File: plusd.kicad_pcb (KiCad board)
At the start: 2 copper layers, 99.1 x 99.1 mm, 63 parts, among them J1 ZX_Spectrum_Connector_GENERIC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, J4 Conn_02x17_Odd_Even, J6 Conn_02x13_Odd_Even, SW1 SW_DPST_x2, SW2 SW_DIP_x02, SW3 SW_DPST_x2, U1 74LS27, U10 74LS374, U11 74LS126, U12 GAL22V10, U2 PAL20L8, U3 74LS00, U4 L7805, U5 AT28C256, U6 6264, U7 WD1772, U8 74LS175, U9 74LS06, Y1 8.000Mhz

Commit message: ahora con joystick
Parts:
- moved R7 0.64 mm to (74.3, 61.0)
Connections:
- J4 pad 26: /DS1 -> /TRACK_0
- R6 pad 1: /DS1 -> /TRACK_0
- U7 pad 23: /DS1 -> /TRACK_0
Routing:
- net /DS1: track 104.3 -> 54.0 mm
- net /TRACK_0: track 0.00 -> 45.6 mm
- net Net-(JP4-Pad1): track 13.1 -> 7.22 mm
- net Net-(C17-Pad2): track 35.9 -> 36.7 mm

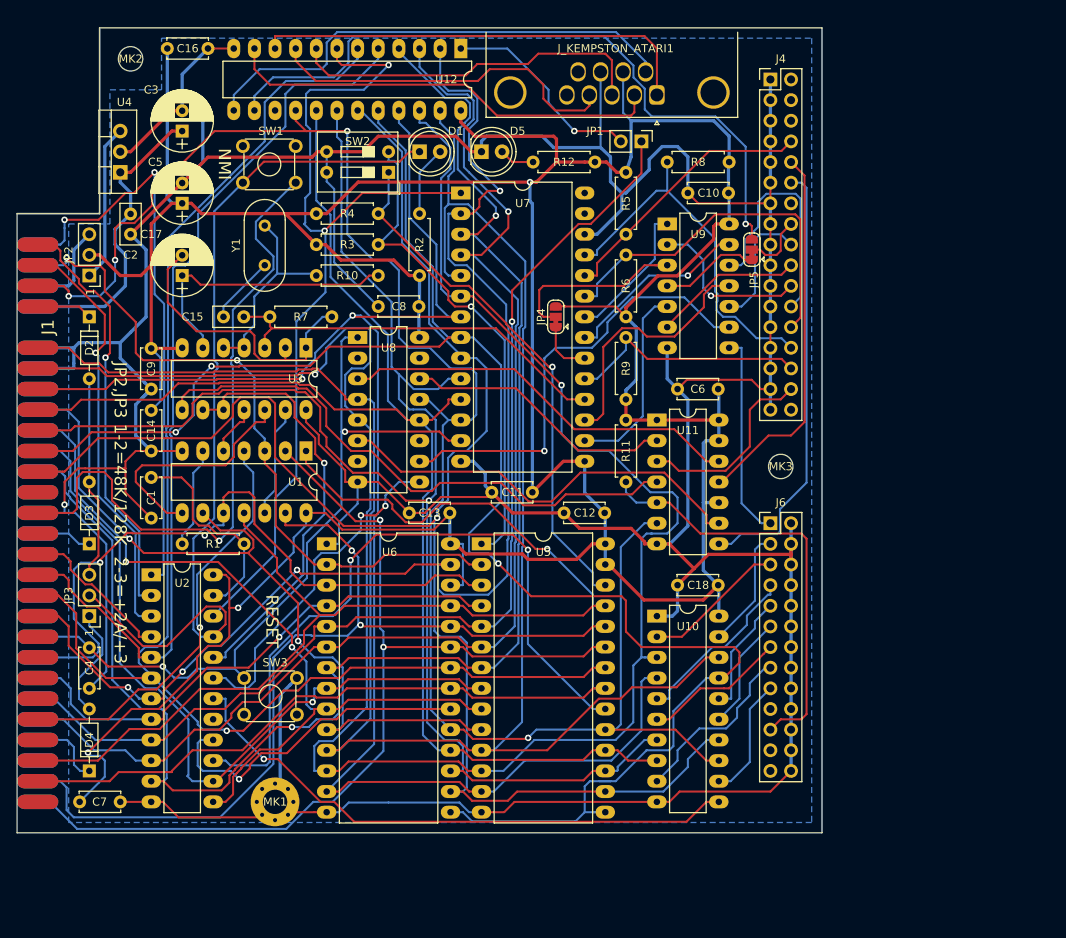
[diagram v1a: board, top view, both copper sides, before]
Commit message: add cable jumpers
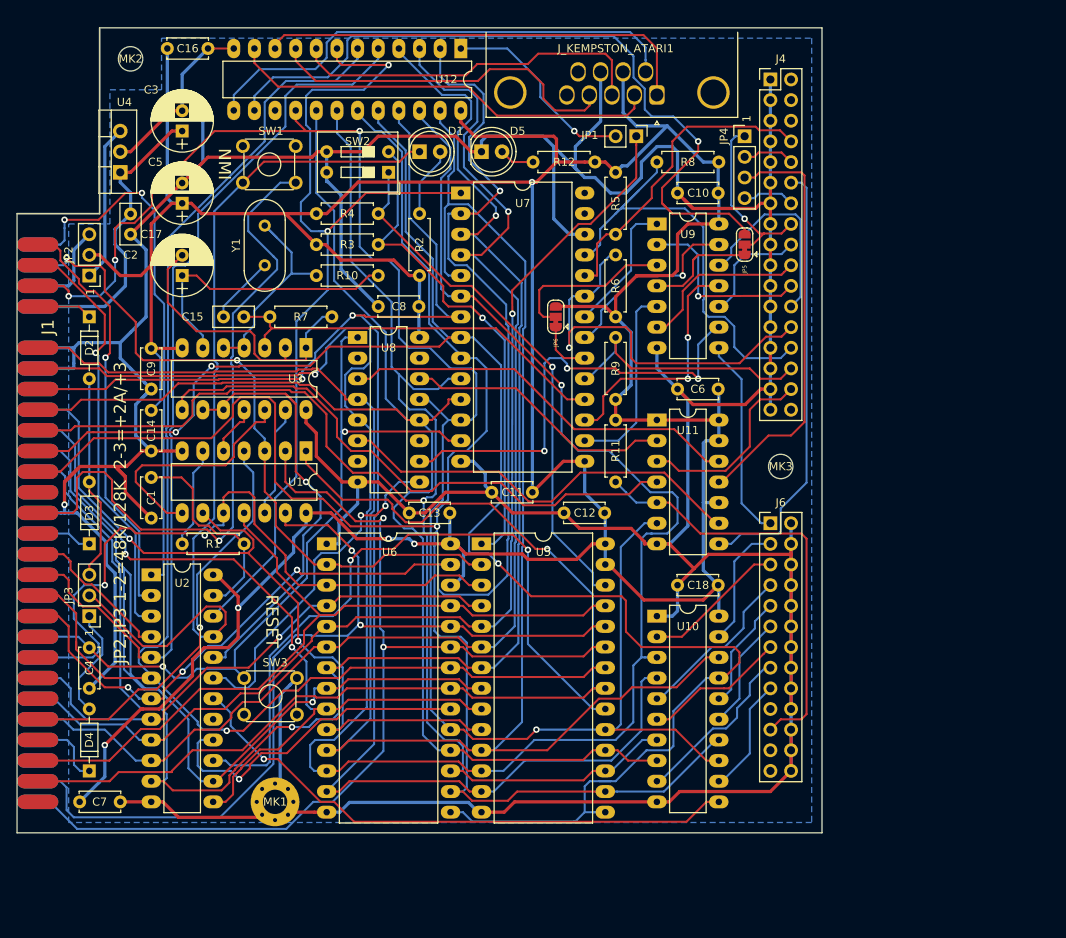
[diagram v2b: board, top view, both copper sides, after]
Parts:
- added JP4: Conn_01x04_Male, Connector_PinHeader_2.54mm:PinHeader_1x04_P2.54mm_Vertical, F.Cu at (125.1, 38.7)
- moved C10 1.27 mm to (116.8, 45.7)
- moved R11 1.27 mm to (109.2, 81.3)
- moved R5 1.27 mm to (109.2, 50.8)
- moved R6 1.27 mm to (109.2, 53.3)
- moved R8 1.27 mm to (114.3, 41.9)
- moved R9 1.27 mm to (109.2, 63.5)
- moved U9 1.27 mm to (114.3, 49.5)
- moved JP5 1.08 mm to (125.1, 52.1)
- moved JP1 0.90 mm to (111.8, 38.7)
- renumbered JP4 to JP6
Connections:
- J4 pad 10: /DS0 -> Net-(J2-Pad2)
- J4 pad 14: (no net) -> Net-(J2-Pad4)
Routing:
- net /A2: track 93.3 -> 116.3 mm
- net /MOTOR_ON: track 7.86 -> 22.1 mm, vias 0 -> 1
- net GND: track 658.0 -> 670.8 mm
- net Net-(J4-Pad28): track 45.7 -> 56.3 mm
- net Net-(J2-Pad4): track 0.00 -> 6.43 mm
- net Net-(J2-Pad2): track 0.00 -> 6.43 mm
- net ALT_MOTOR_ON: track 86.8 -> 92.4 mm
- net /INDEX: track 33.1 -> 38.6 mm
- net /DS0: track 46.3 -> 51.7 mm
- net Net-(J4-Pad24): track 29.8 -> 24.7 mm
- net /D6: track 171.9 -> 176.9 mm
- net /TRACK_0: track 45.6 -> 50.4 mm, vias 0 -> 1
- net /A14: track 71.2 -> 66.7 mm
- net /A11: track 120.1 -> 123.2 mm
- net Net-(J4-Pad30): track 30.0 -> 33.1 mm
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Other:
- net class power: trace_width 0.35 -> 0.4

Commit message: fix power to chips
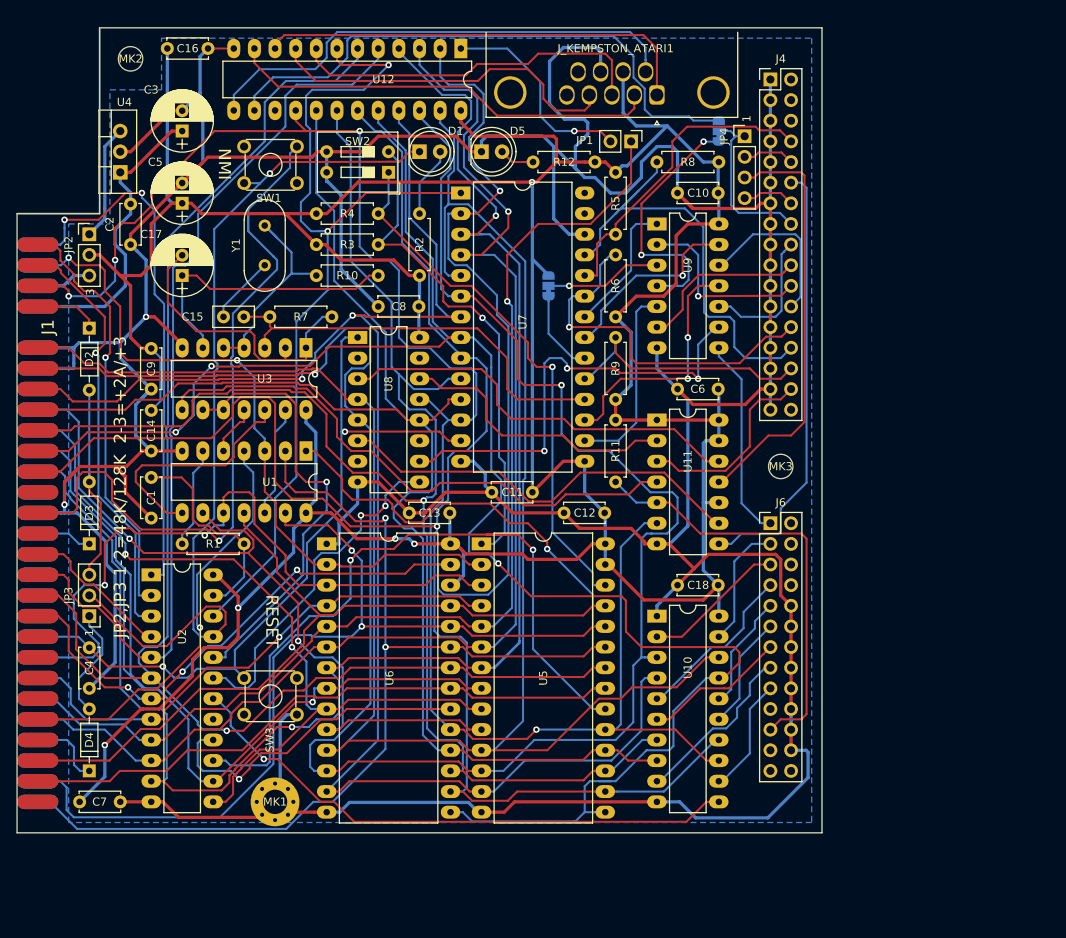
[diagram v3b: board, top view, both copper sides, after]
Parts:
- C2: value 10n -> 100n; footprint Capacitors_THT:C_Disc_D5.0mm_W2.5mm_P2.50mm -> Capacitors_THT:C_Disc_D5.0mm_W2.5mm_P5.00mm
- JP5, JP6: moved to B.Cu
- R12, R2: value 2K2 -> 680
- SW1, SW3: footprint Buttons_Switches_THT:SW_TH_Tactile_Omron_B3F-10xx -> SINCLAIR:SW_TH_Tactile_Omron_B3F-10xx
- moved JP5 14.3 mm to (121.9, 38.1)
- moved SW1 7.75 mm to (63.5, 40.0), turned to 0 degrees
- moved JP2 5.08 mm to (44.5, 50.8), turned to 0 degrees
- moved JP6 3.91 mm to (101.0, 57.1)
- moved D2 1.40 mm to (44.5, 62.4)
- moved C2 1.27 mm to (49.5, 52.1)
- moved JP1 0.90 mm to (111.1, 39.4)
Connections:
- J6 pad 2: GND -> (no net)
- J6 pad 26: GND -> (no net)
- J6 pad 4: GND -> (no net)
- J6 pad 6: GND -> (no net)
- J6 pad 8: GND -> (no net)
- SW3 pad 1: /RESET -> (no net)
- SW3 pad 2: GND -> (no net)
- SW3 pad 3: (no net) -> /RESET
- SW3 pad 4: (no net) -> GND
- U3 pad 14: GND -> +5V
- U3 pad 7: +5V -> GND
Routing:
- net GND: track 670.8 -> 639.1 mm, vias 1 -> 2
- net ALT_MOTOR_ON: track 92.4 -> 70.6 mm, vias 1 -> 0
- net Net-(JP5-Pad1): track 14.2 -> 31.7 mm, vias 0 -> 2
- net /A3: track 197.8 -> 207.5 mm
- net Net-(JP6-Pad2): track 21.0 -> 14.6 mm, vias 0 -> 1
- net NMI: track 83.8 -> 89.4 mm
- net Net-(JP2-Pad1): track 19.4 -> 13.8 mm
- net /TRACK_0: track 50.4 -> 45.7 mm
- net plus3_5V: track 11.2 -> 6.88 mm
- net Net-(J4-Pad24): track 24.7 -> 20.6 mm
- net ROM_CS: track 86.4 -> 89.9 mm
- net Net-(JP6-Pad1): track 7.22 -> 10.3 mm
- net /DIR: track 14.1 -> 17.2 mm
- net /A4: track 155.6 -> 158.4 mm
- net /D1: track 251.1 -> 253.8 mm
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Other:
- board text added: "1773 1772"
- board text added: "3"
- board text added: "EMU REAL"
- board text added: "Expecial Edicion for www.va-de-retro.com"
- board text removed: "Edicion para www.va-de-retro.com"

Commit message: add schematic and BOM
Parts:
- removed MK3: Mounting_Hole, MountingHole:MountingHole_3mm
- added JP7: Conn_02x02_Odd_Even, Connector_PinHeader_2.54mm:PinHeader_2x02_P2.54mm_Vertical, F.Cu at (129.0, 81.5)
- SW1, SW3: footprint SINCLAIR:SW_TH_Tactile_Omron_B3F-10xx -> Buttons_Switches_THT:SW_TH_Tactile_Omron_B3F-10xx
- moved J_KEMPSTON_ATARI1 1.91 mm to (114.3, 31.8)
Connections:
- U11 pad 11: /DS0 -> Net-(JP7-Pad3)
- U11 pad 8: /DS1 -> Net-(JP7-Pad2)
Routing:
- net Net-(JP7-Pad2): track 0.00 -> 15.4 mm
- net /DS1: track 54.0 -> 40.8 mm
- net Net-(JP7-Pad3): track 0.00 -> 8.42 mm
- net /DS0: track 51.7 -> 46.3 mm
- net +5V: track 502.7 -> 504.7 mm
- net J4-Right: track 44.0 -> 45.9 mm
- net J2-Down: track 53.2 -> 55.1 mm
- net J1-Up: track 54.4 -> 52.5 mm
- net ALT_MOTOR_ON: track 70.6 -> 71.6 mm
- net J3-Left: track 44.3 -> 45.0 mm
- net J6-Fire: track 60.7 -> 61.2 mm

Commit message: correcciones esteticas
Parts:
- added REF***: KiCad-Logo2_6mm_B_SilkScreen, SINCLAIR:KiCad-Logo2_6mm_B_SilkScreen, F.Cu at (98.0, 71.1)
- moved J_KEMPSTON_ATARI1 1.52 mm to (115.8, 31.8)
- moved JP4 0.65 mm to (125.0, 38.1)
- moved R12 0.51 mm to (98.6, 41.9)
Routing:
- net ALT_MOTOR_ON: track 71.6 -> 75.9 mm
- net J4-Right: track 45.9 -> 49.4 mm
- net GND: track 638.6 -> 641.6 mm
- net Net-(J4-Pad10): track 6.43 -> 9.23 mm
- net J1-Up: track 52.5 -> 55.2 mm
- net Net-(J4-Pad14): track 6.50 -> 8.91 mm
- net J3-Left: track 45.0 -> 47.1 mm
- net J2-Down: track 55.1 -> 56.9 mm
- net +5V: track 504.7 -> 503.1 mm
- net /DS0: track 46.3 -> 47.5 mm
- net /INDEX: track 38.6 -> 39.5 mm
- net /A1: track 99.2 -> 100.0 mm
- net Net-(JP1-Pad2): track 25.6 -> 26.4 mm
- net /A0: track 97.0 -> 97.6 mm
- net ROM_CS: track 89.9 -> 90.5 mm
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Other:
- board text added: "2"

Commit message: aestetical changes
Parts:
- removed the REF*** at (98.0, 71.1)
- added REF***: OSHW-Logo_5.7x6mm_SilkScreen, Symbols:OSHW-Logo_5.7x6mm_SilkScreen, B.Cu at (97.9, 49.7)
- added REF***: KiCad-Logo2_6mm_SilkScreen, Symbols:KiCad-Logo2_6mm_SilkScreen, B.Cu at (97.9, 70.1)
- added SW1: SW_DPST_x2, SINCLAIR:SW_TH_Tactile_Omron_B3F-10xx, F.Cu at (69.6, 134.5)
- moved JP7 0.60 mm to (129.5, 81.3)
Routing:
- net GND: track 641.6 -> 620.5 mm
- net /D1: track 253.8 -> 257.2 mm
- net Net-(JP7-Pad2): track 15.4 -> 18.3 mm
- net Net-(J5-Pad6): track 14.1 -> 16.5 mm
- net /DS1: track 40.8 -> 43.0 mm
- net Net-(J5-Pad4): track 20.9 -> 22.6 mm
- net /DS0: track 47.5 -> 46.4 mm
- net Net-(J5-Pad5): track 14.3 -> 15.3 mm
- net Net-(U8-Pad10): track 54.9 -> 55.8 mm
- net Net-(J5-Pad8): track 21.3 -> 22.0 mm
- net /D3: track 220.4 -> 219.7 mm

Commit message: a
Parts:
- removed the JP1 at (111.1, 39.4)
- removed J_KEMPSTON_ATARI1: DB9_Male, Connector_Dsub:DSUB-9_Male_Horizontal_P2.77x2.84mm_EdgePinOffset4.94mm_Housed_MountingHolesOffset7.48mm
- removed the R12 at (98.6, 41.9)
- removed the R3 at (80.0, 52.1)
- removed the SW1 at (63.5, 40.0)
- removed the SW1 at (69.6, 134.5)
- removed the SW2 at (81.3, 43.2)
- removed U9: 74LS06, Housings_DIP:DIP-14_W7.62mm_LongPads
- added IC5: 74LS06, Housings_DIP:DIP-14_W7.62mm_LongPads, F.Cu at (87.6, 45.7)
- added J2: Conn_02x17_Odd_Even, Connector_PinHeader_2.54mm:PinHeader_2x17_P2.54mm_Vertical, F.Cu at (69.8, 31.8)
- added MK3: Mounting_Hole, MountingHole:MountingHole_3mm, F.Cu at (76.5, 49.8)
- added R11: 10K, Resistors_THT:R_Axial_DIN0207_L6.3mm_D2.5mm_P7.62mm_Horizontal, F.Cu at (94.0, 80.0)
- added R8: 2K2, Resistors_THT:R_Axial_DIN0207_L6.3mm_D2.5mm_P7.62mm_Horizontal, F.Cu at (87.1, 92.5)
- added SLOT: MountingHole_1mm, SINCLAIR:MountingHole_1mm, F.Cu at (68.8, 114.8)
- added SLOT: MountingHole_1mm, SINCLAIR:MountingHole_1mm, F.Cu at (66.8, 114.8)
- added SLOT: MountingHole_1mm, SINCLAIR:MountingHole_1mm, F.Cu at (64.8, 114.8)
- added SW1: SW_DPST_x2, Buttons_Switches_THT:SW_TH_Tactile_Omron_B3F-10xx, F.Cu at (78.1, 96.5)
- added SW3: SW_DIP_x03, Button_Switch_THT:SW_DIP_SPSTx03_Slide_6.7x9.18mm_W7.62mm_P2.54mm_LowProfile, F.Cu at (78.7, 86.4)
- C13: renamed from C15; footprint Capacitors_THT:C_Disc_D5.0mm_W2.5mm_P2.50mm -> Capacitor_THT:C_Disc_D5.0mm_W2.5mm_P5.00mm
- IC4: renamed from U2; value PAL20L8 -> GAL20V8
- J4: value Conn_02x17_Odd_Even -> DB9_Male; footprint Connector_PinHeader_2.54mm:PinHeader_2x17_P2.54mm_Vertical -> Connector_Dsub:DSUB-9_Male_Horizontal_P2.77x2.84mm_EdgePinOffset4.94mm_Housed_MountingHolesOffset7.48mm
- R10: value 2K2 -> 680
- Y1: footprint Crystals:Crystal_HC49-U_Vertical -> Crystal:Crystal_HC18-U_Vertical
- moved C4 110.8 mm to (158.8, 111.8), turned to 270 degrees
- moved D2 110.5 mm to (154.9, 115.6), turned to 180 degrees
- moved C16 100.7 mm to (144.8, 115.6), turned to 180 degrees
- moved MK1 95.6 mm to (158.8, 92.7), turned to 90 degrees
- moved JP2 93.2 mm to (135.9, 115.6), turned to 270 degrees
- moved J1 89.3 mm to (115.6, 121.9), turned to 0 degrees
- moved D3 86.8 mm to (127.0, 115.6), turned to 180 degrees
- moved MK2 83.2 mm to (67.3, 110.5), turned to 90 degrees
- moved SW2 80.5 mm to (143.5, 96.5), turned to 90 degrees
- moved IC4 80.2 mm to (130.8, 108.0), turned to 90 degrees
- moved JP1 78.6 mm to (88.9, 115.6), turned to 90 degrees
- moved D4 77.3 mm to (100.5, 115.6), turned to 0 degrees
- moved IC12 76.1 mm to (81.3, 111.8), turned to 180 degrees
- moved C12 73.4 mm to (66.0, 101.0), turned to 270 degrees
- moved C1 71.2 mm to (90.2, 110.5), turned to 180 degrees
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- renumbered C2 to C1, C13 to C10, C14 to C11, C16 to C12, C17 to C14, C1 to C15, C4 to C16, C3 to C17, C5 to C18, C6 to C2, C18 to C3, C7 to C4, C8 to C5, C9 to C6, C10 to C7, C11 to C8, C12 to C9, D4 to D2, D2 to D4, U7 to IC1, U1 to IC10, U12 to IC11, U4 to IC12, U5 to IC2, U6 to IC3, U11 to IC6, U10 to IC7, U8 to IC8, U3 to IC9, J6 to J3, JP2 to JP1, JP3 to JP2, JP7 to JP5, JP5 to JP7, R5 to R1, R4 to R12, R6 to R2, R8 to R3, R9 to R4, R11 to R5, R2 to R6, R1 to R9, SW3 to SW2
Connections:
- C14 pad 1: Net-(C17-Pad1) -> Net-(C14-Pad1)
- IC1 pad 19: Net-(J4-Pad30) -> Net-(IC1-Pad19)
- IC1 pad 25: Net-(J4-Pad28) -> Net-(IC1-Pad25)
- IC10 pad 12: Net-(U1-Pad12) -> Net-(IC10-Pad12)
- IC10 pad 8: Net-(U1-Pad8) -> Net-(IC10-Pad8)
- IC11 pad 1: Net-(JP1-Pad2) -> JOY_EN
- IC9 pad 12: Net-(U1-Pad8) -> Net-(IC10-Pad12)
- IC9 pad 13: Net-(U1-Pad12) -> Net-(IC10-Pad8)
- IC9 pad 4: Net-(R10-Pad1) -> Net-(IC9-Pad4)
- IC9 pad 5: Net-(R10-Pad1) -> Net-(IC9-Pad4)
- IC9 pad 6: Net-(C17-Pad1) -> Net-(C14-Pad1)
- J4 pad 1: GND -> J1-Up
- J4 pad 2: (no net) -> J2-Down
- J4 pad 3: GND -> J3-Left
- J4 pad 4: (no net) -> J4-Right
- J4 pad 5: GND -> (no net)
- J4 pad 6: (no net) -> J6-Fire
- J4 pad 7: GND -> +5V
- J4 pad 8: /INDEX -> GND
- J4 pad 9: GND -> (no net)
- JP4 pad 2: Net-(J4-Pad10) -> Net-(J2-Pad10)
- JP4 pad 4: Net-(J4-Pad14) -> Net-(J2-Pad14)
- R10 pad 1: Net-(R10-Pad1) -> Net-(D5-Pad2)
- R10 pad 2: Net-(C17-Pad1) -> +5V
- R3 pad 1: Net-(J4-Pad28) -> Net-(IC1-Pad25)
- R4 pad 1: Net-(J4-Pad30) -> Net-(IC1-Pad19)
- Y1 pad 2: Net-(R10-Pad1) -> Net-(IC9-Pad4)
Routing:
- net /D1: track 257.2 -> 200.4 mm, vias 2 -> 3
- net Net-(J4-Pad28): track 56.5 -> 0.00 mm
- net Net-(IC1-Pad25): track 0.00 -> 52.3 mm
- net /D0: track 243.2 -> 197.3 mm, vias 0 -> 2
- net Net-(C17-Pad1): track 35.4 -> 0.00 mm
- net Net-(IC1-Pad19): track 0.00 -> 34.0 mm
- net JOY_EN: track 0.00 -> 33.7 mm, vias 0 -> 2
- net Net-(J4-Pad30): track 33.1 -> 0.00 mm
- net Net-(U1-Pad8): track 29.4 -> 0.00 mm
- net Net-(R10-Pad1): track 26.7 -> 0.00 mm
- net Net-(JP1-Pad2): track 26.4 -> 0.00 mm, vias 1 -> 0
- net Net-(C14-Pad1): track 0.00 -> 24.1 mm
- net Net-(IC9-Pad4): track 0.00 -> 23.8 mm
- net Net-(IC10-Pad8): track 0.00 -> 23.0 mm, vias 0 -> 2
- net Net-(J4-Pad22): track 22.6 -> 0.00 mm, vias 1 -> 0
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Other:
- outline, holes or cut-outs redrawn
- net class Default: trace_width 0.25 -> 0.2
- board text added: "(2-3) +2A/+3 48K/128K (1-2)"
- board text added: "+2A/+3 (2-3)"
- board text added: "1-2,3-4 AT 2-3 SH"
- board text added: "NOR || INV ="
- board text added: "Special edition for www.va-de-retro.com"
- board text removed: "Expecial Edicion for www.va-de-retro.com"
- board text removed: "JP2,JP3 1-2=48K/128K 2-3=+2A/+3"

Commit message: añadido ibom
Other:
- net class Default removed
- net class power removed
